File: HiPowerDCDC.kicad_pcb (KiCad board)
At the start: 2 copper layers, 105.2 x 100 mm, 57 parts, among them J1 Conn_01x01, J2 Conn_01x01, J3 Conn_01x01, J4 Conn_01x01, J5 Conn_01x04, Q1 WMJ38N60, Q2 WMJ38N60, SW1 SW_Push, SW2 SW_Push, U1 ESP32-WROOM-32U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

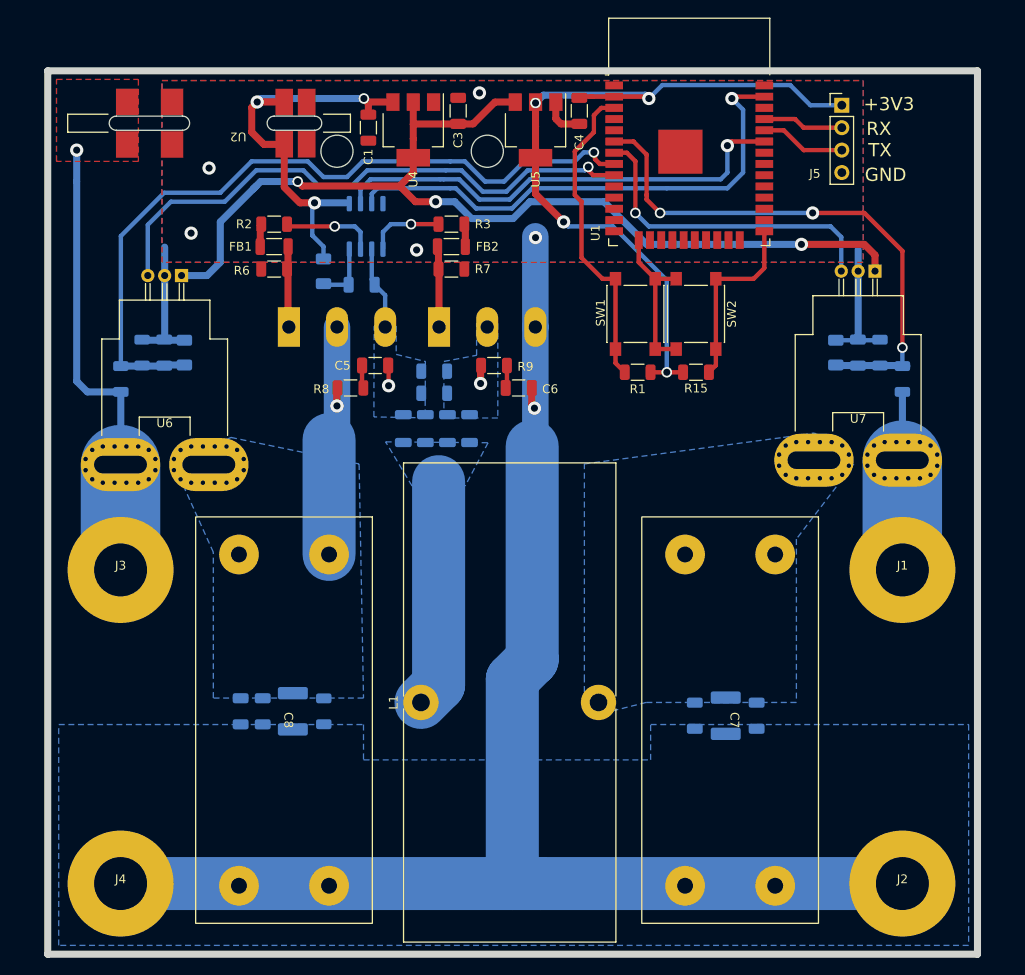
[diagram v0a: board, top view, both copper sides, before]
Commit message: Modified HV tracks and cleaned up PCB
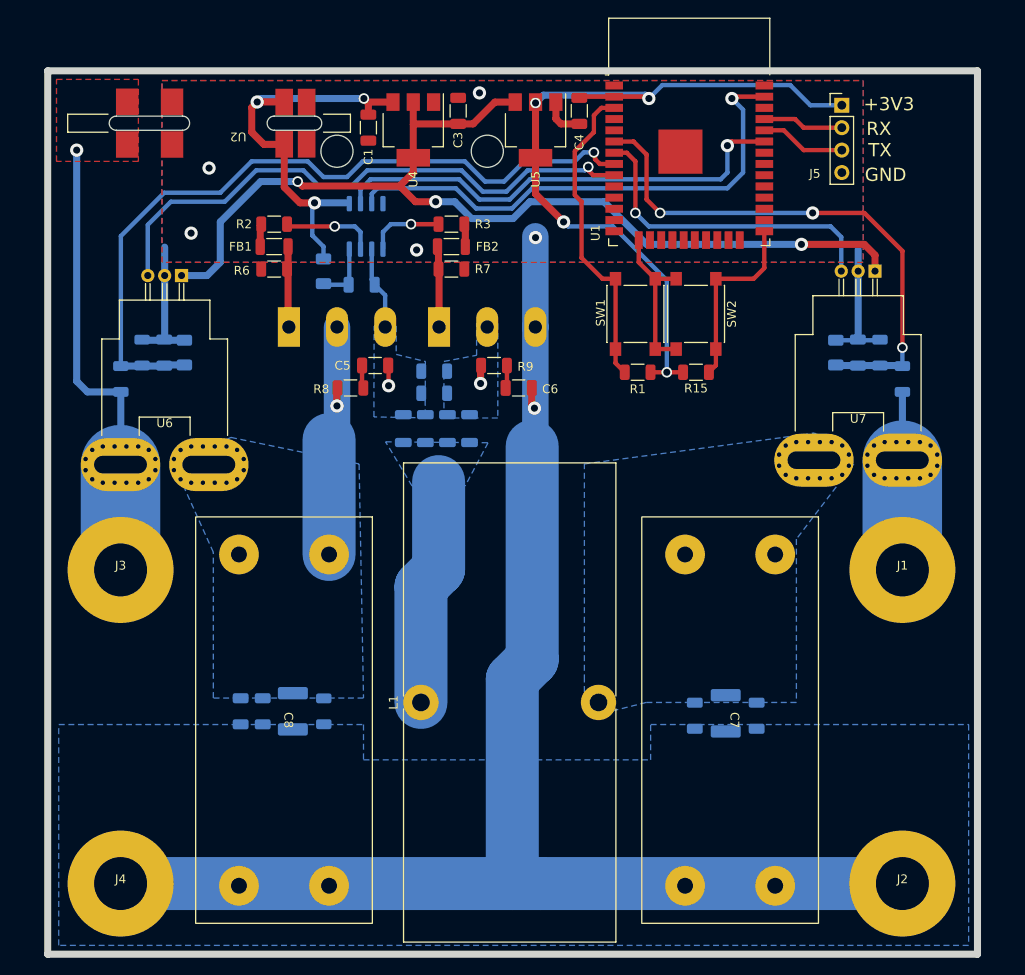
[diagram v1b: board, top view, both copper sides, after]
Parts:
- moved C9 0.27 mm to (186.5, 125.7)
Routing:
- net Net-(J1-Pad1): track 21.8 -> 20.4 mm
- net VDC: track 52.7 -> 51.8 mm
- net +12V: track 48.1 -> 47.3 mm

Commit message: Added ACDC 3d model, reorganized switching FETs
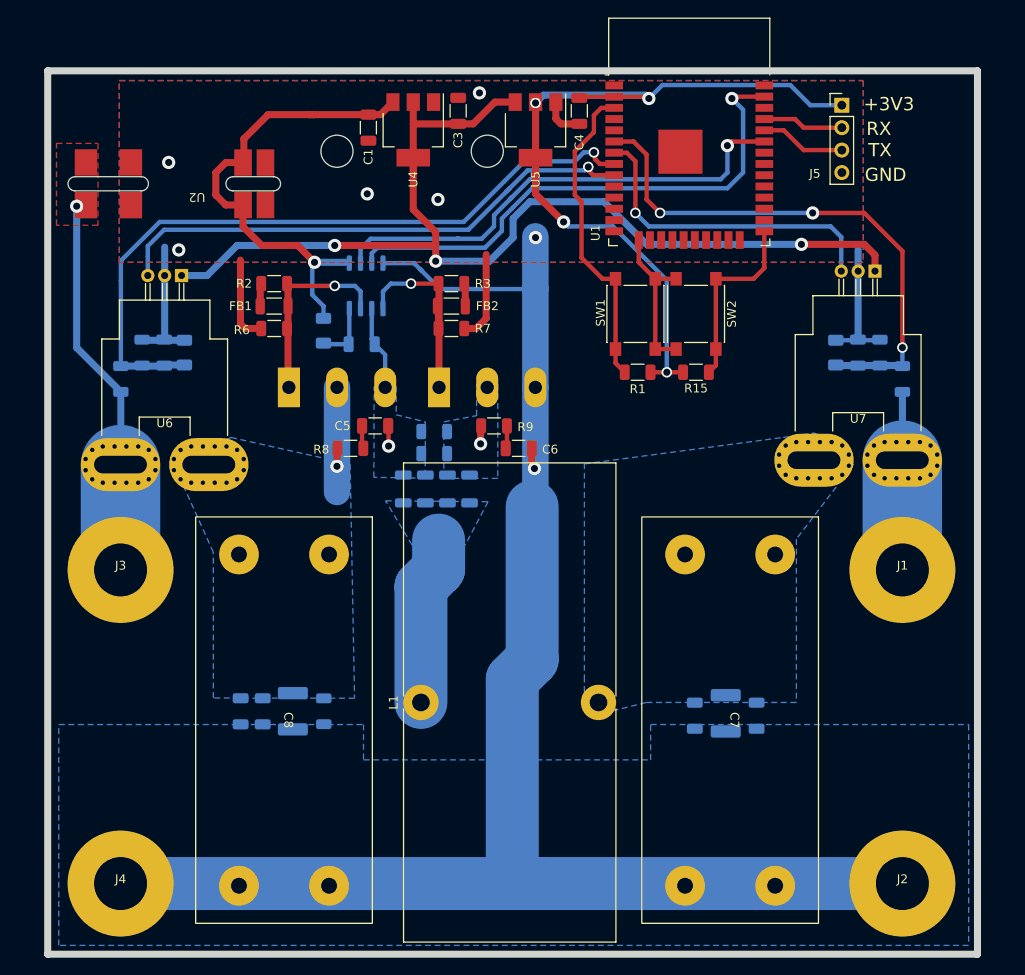
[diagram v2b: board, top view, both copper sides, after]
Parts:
- moved U2 8.29 mm to (126.1, 65.8)
- moved C5 6.83 mm to (146.8, 93.2)
- moved C6 6.83 mm to (163.1, 95.7)
- moved FB3 6.83 mm to (152.5, 100.3)
- moved FB4 6.83 mm to (157.5, 100.3)
- moved FB5 6.83 mm to (150.0, 100.3)
- moved FB6 6.83 mm to (155.0, 100.3)
- moved Q1 6.83 mm to (137.1, 88.8)
- moved Q2 6.83 mm to (154.1, 88.8)
- moved R4 6.83 mm to (153.5, 96.3)
- moved R5 6.83 mm to (153.5, 93.8)
- moved R8 6.83 mm to (144.0, 95.7)
- moved R9 6.83 mm to (160.3, 93.2)
- moved C2 6.73 mm to (145.3, 83.9)
- moved D1 6.73 mm to (141.0, 82.4)
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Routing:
- net GND: track 218.8 -> 257.4 mm, vias 6 -> 7
- net VCC: track 28.2 -> 13.9 mm
- net VDC: track 51.8 -> 43.3 mm
- net +12V: track 47.3 -> 54.1 mm, vias 3 -> 1
- net Net-(FB3-Pad2): track 25.8 -> 19.2 mm
- net +5V: track 115.1 -> 121.7 mm
- net VIN: track 86.1 -> 81.1 mm
- net Net-(FB2-Pad2): track 9.18 -> 13.9 mm
- net CIN: track 65.3 -> 60.9 mm
- net Net-(U1-Pad33): track 53.3 -> 55.5 mm
- net Net-(U1-Pad37): track 58.7 -> 60.4 mm

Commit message: Placed mounting holes
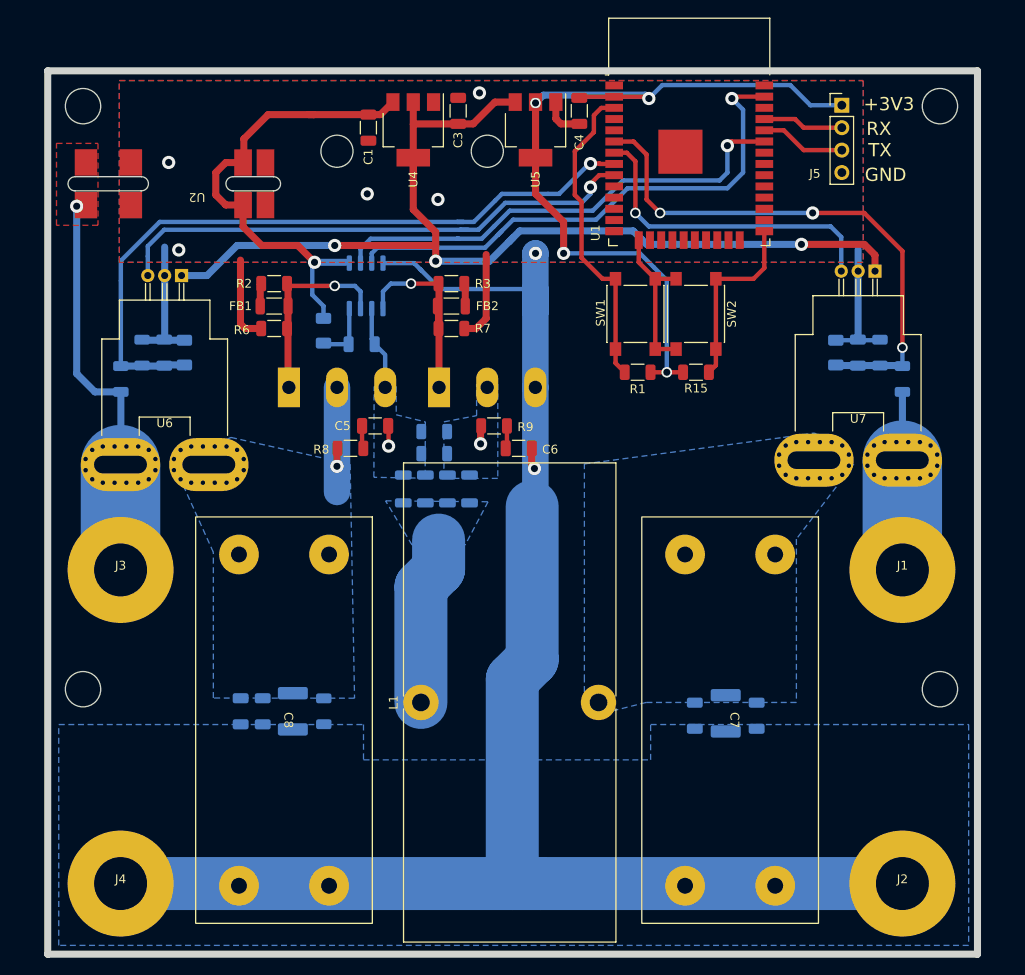
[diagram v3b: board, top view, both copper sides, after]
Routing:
- net +5V: track 121.7 -> 118.3 mm
- net +3V3: track 88.7 -> 90.8 mm
- net VDC: track 43.3 -> 45.0 mm
- net VIN: track 81.1 -> 79.7 mm
- net Net-(U1-Pad33): track 55.5 -> 54.4 mm
- net GND: track 257.4 -> 258.0 mm
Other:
- outline, holes or cut-outs redrawn

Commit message: Changed to high voltage capacitors
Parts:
- C11, C12, C13, C14: footprint Capacitor_SMD:C_1206_3216Metric -> Capacitor_SMD:C_1812_4532Metric
- R10: footprint Resistor_SMD:R_1206_3216Metric -> Resistor_SMD:R_1812_4532Metric
- moved C13 2.45 mm to (180.6, 126.0)
- moved C9 1.97 mm to (184.6, 126.0)
- moved R10 1.55 mm to (142.6, 125.6)
- moved C11 1.45 mm to (188.6, 126.0)
- moved C10 1.05 mm to (138.6, 125.6)
- moved C14 1.04 mm to (130.6, 125.6)
- moved C12 0.47 mm to (134.6, 125.6)
- moved FB3 0.15 mm to (152.3, 100.3)
- moved FB4 0.15 mm to (157.3, 100.3)
- moved FB5 0.15 mm to (149.8, 100.3)
- moved FB6 0.15 mm to (154.8, 100.3)
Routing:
- net Net-(R2-Pad1): track 10.6 -> 0.00 mm, vias 1 -> 0
- net Net-(FB1-Pad2): track 9.14 -> 19.8 mm, vias 0 -> 1
- net Net-(R3-Pad1): track 8.59 -> 0.00 mm, vias 1 -> 0
- net Net-(FB2-Pad2): track 13.9 -> 22.5 mm, vias 0 -> 1
- net VCC: track 13.9 -> 17.0 mm
- net Net-(FB4-Pad2): track 2.06 -> 4.50 mm
- net Net-(C2-Pad1): track 11.9 -> 13.6 mm
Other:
- board text added: "BOOT"
- board text added: "RST"

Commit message: Laci, check this out
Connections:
- R2 pad 1: Net-(R2-Pad1) -> Net-(FB1-Pad2)
- R3 pad 1: Net-(R3-Pad1) -> Net-(FB2-Pad2)
- U3 pad 5: Net-(R3-Pad1) -> Net-(FB2-Pad2)
- U3 pad 7: Net-(R2-Pad1) -> Net-(FB1-Pad2)
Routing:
- net Net-(J5-Pad3): track 9.70 -> 11.4 mm
- net CIN: track 61.0 -> 59.7 mm
- net GND: track 258.0 -> 257.1 mm, vias 7 -> 6
- net Net-(FB2-Pad2): track 22.5 -> 21.8 mm

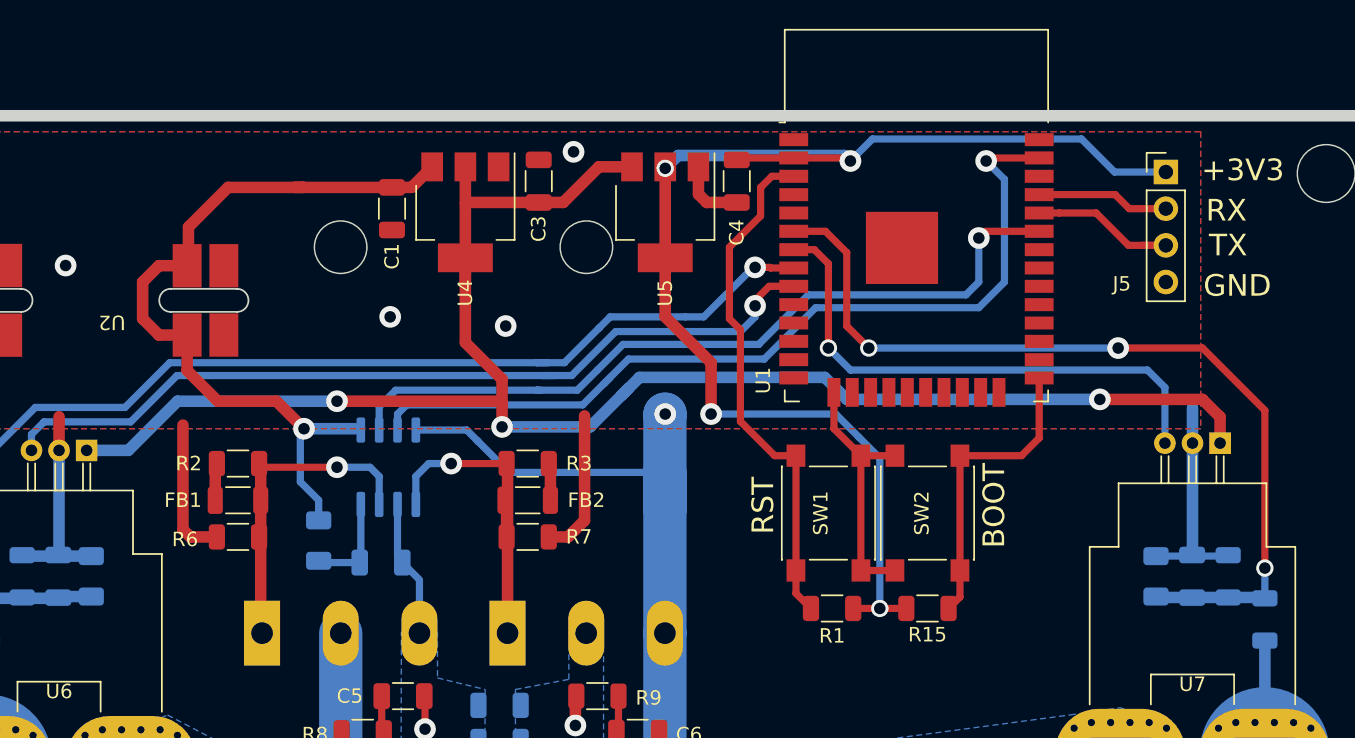
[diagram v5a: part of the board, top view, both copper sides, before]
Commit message: Added PTC sensor, Laci you didn't check me :(
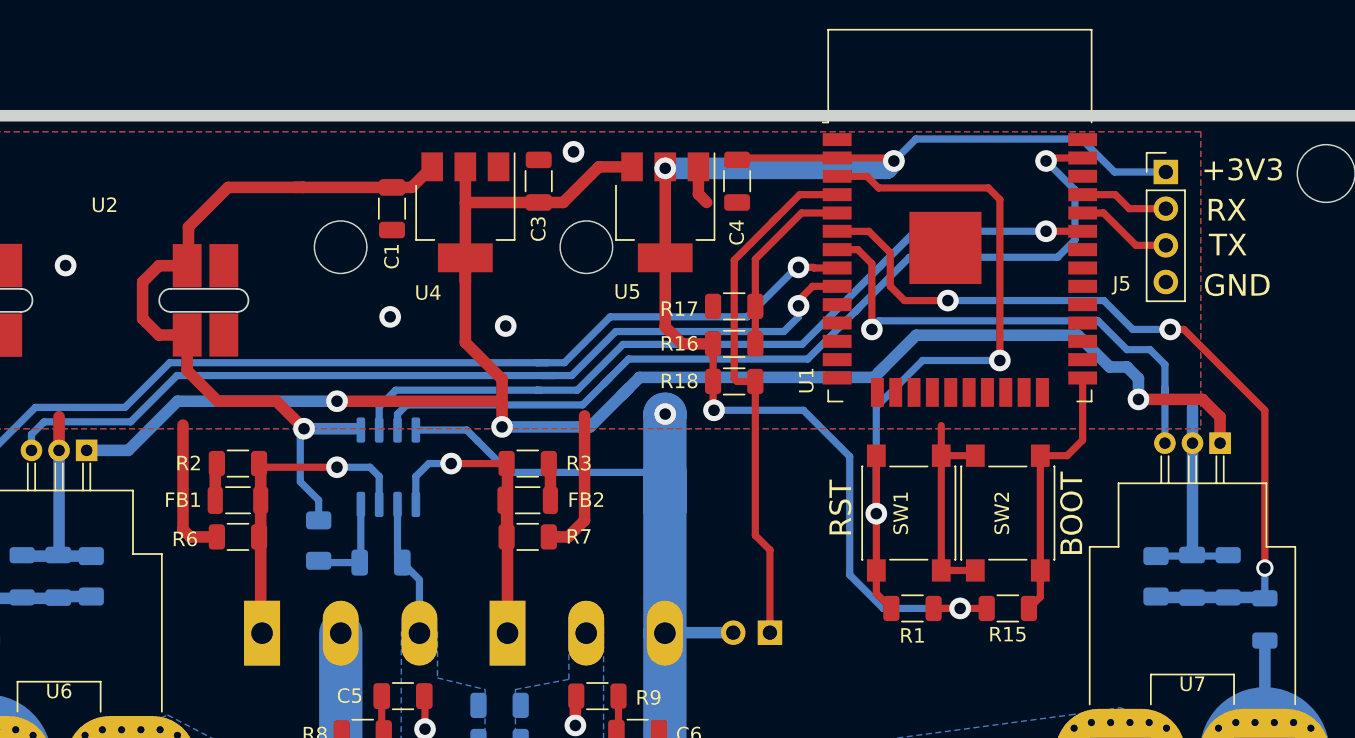
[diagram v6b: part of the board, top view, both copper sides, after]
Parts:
- added R16: 10k, Resistor_SMD:R_1206_3216Metric, F.Cu at (169.8, 68.8)
- added R17: 10k, Resistor_SMD:R_1206_3216Metric, F.Cu at (169.8, 66.2)
- added R18: 1M, Resistor_SMD:R_1206_3216Metric, F.Cu at (169.8, 71.4)
- added TH1: Thermistor_PTC, Connector_PinHeader_2.54mm:PinHeader_1x02_P2.54mm_Vertical, B.Cu at (172.2, 88.8)
- moved R1 5.57 mm to (182.1, 87.1)
- moved R15 5.57 mm to (188.7, 87.1)
- moved SW1 5.57 mm to (181.8, 80.5)
- moved SW2 5.57 mm to (188.7, 80.5)
- moved U1 3.01 mm to (185.4, 62.9)
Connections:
- U1 pad 4: unconnected-(U1-Pad4) -> TEMP
- U1 pad 5: unconnected-(U1-Pad5) -> Net-(U1-Pad5)
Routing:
- net TEMP: track 0.00 -> 37.1 mm
- net Net-(R1-Pad1): track 35.9 -> 51.4 mm, vias 0 -> 2
- net Net-(U1-Pad5): track 0.00 -> 12.9 mm
- net Net-(U1-Pad33): track 54.4 -> 62.2 mm
- net +3V3: track 90.8 -> 98.2 mm
- net +5V: track 118.3 -> 123.1 mm
- net Net-(J5-Pad3): track 11.4 -> 6.69 mm
- net VOUT: track 61.5 -> 56.9 mm
- net VIN: track 79.6 -> 82.6 mm
- net Net-(J5-Pad2): track 9.18 -> 6.17 mm
- net CIN: track 59.7 -> 62.7 mm
- net Net-(U1-Pad37): track 60.2 -> 63.0 mm
- net Net-(R15-Pad1): track 21.1 -> 18.6 mm
- net COUT: track 36.9 -> 35.7 mm

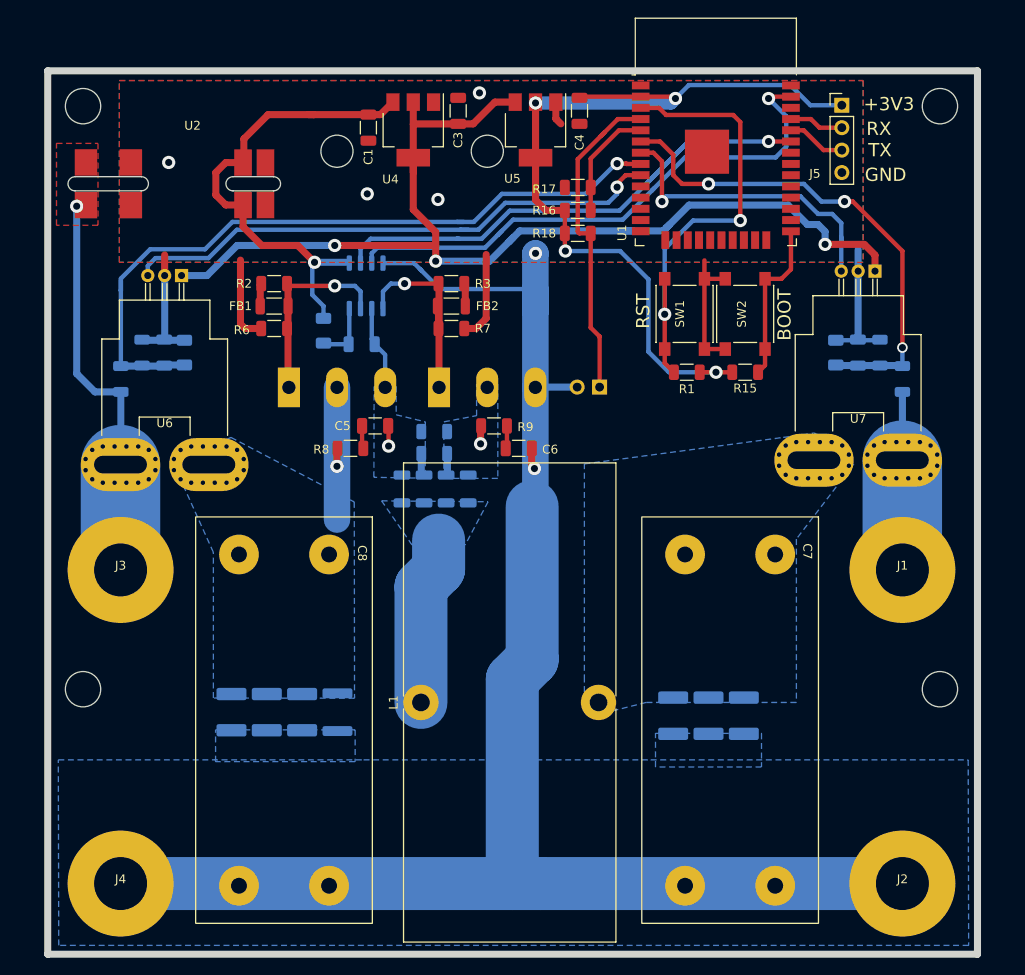
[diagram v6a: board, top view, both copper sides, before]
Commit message: Added Keystone connectors
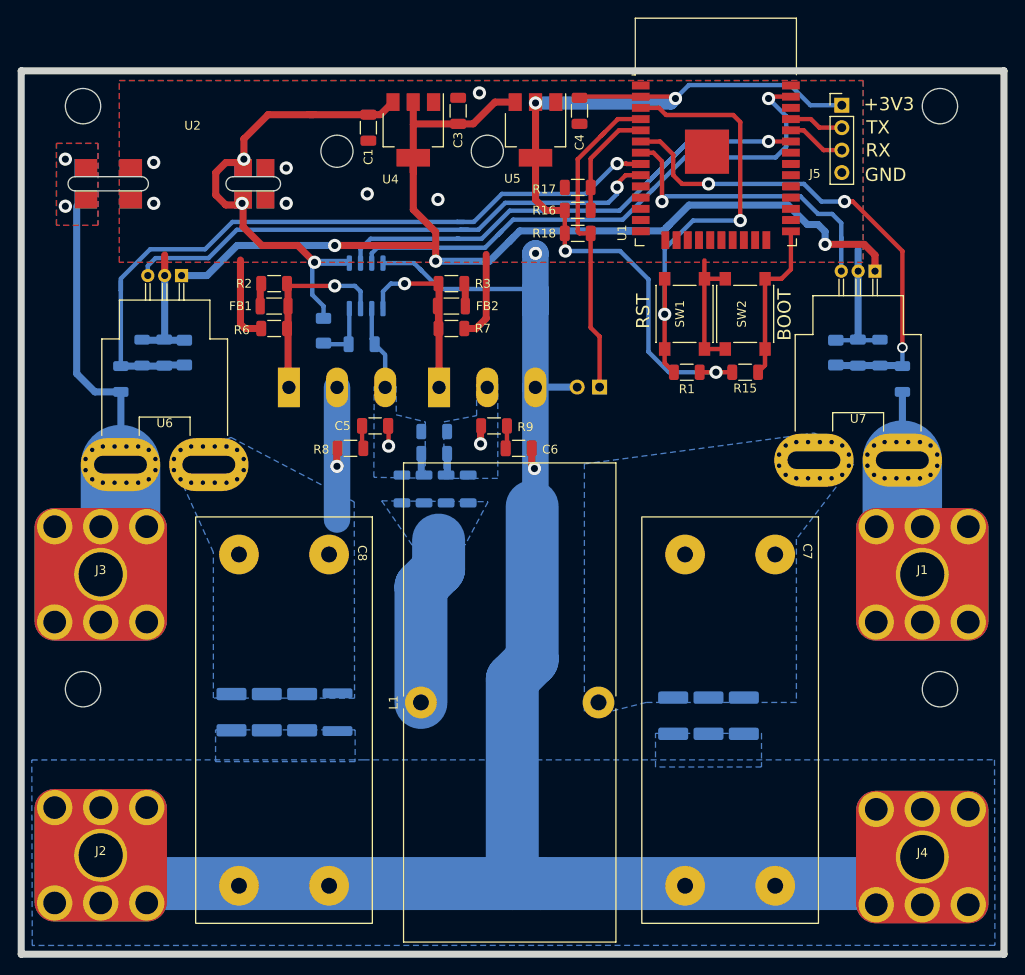
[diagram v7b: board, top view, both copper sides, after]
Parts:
- J1, J2, J3, J4: footprint HiPowerFP:Screw_PCB_pin -> HiPowerFP:Keystone_7808
- moved J2 90.8 mm to (115.8, 141.8)
- moved J4 90.8 mm to (208.8, 142.0)
- moved J1 2.30 mm to (208.8, 110.0)
- moved J3 2.30 mm to (115.8, 110.0)
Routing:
- net VDC: track 45.0 -> 65.8 mm, vias 1 -> 2
- net Net-(J1-Pad1): track 20.4 -> 36.0 mm
- net GND: track 256.7 -> 254.0 mm, vias 6 -> 9
- net +12V: vias 1 -> 3
- added copper zone on B.Cu, net VDC
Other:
- board size 105.2 x 100 mm -> 111.2 x 100 mm
